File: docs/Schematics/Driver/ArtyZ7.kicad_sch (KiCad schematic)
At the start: 0 parts

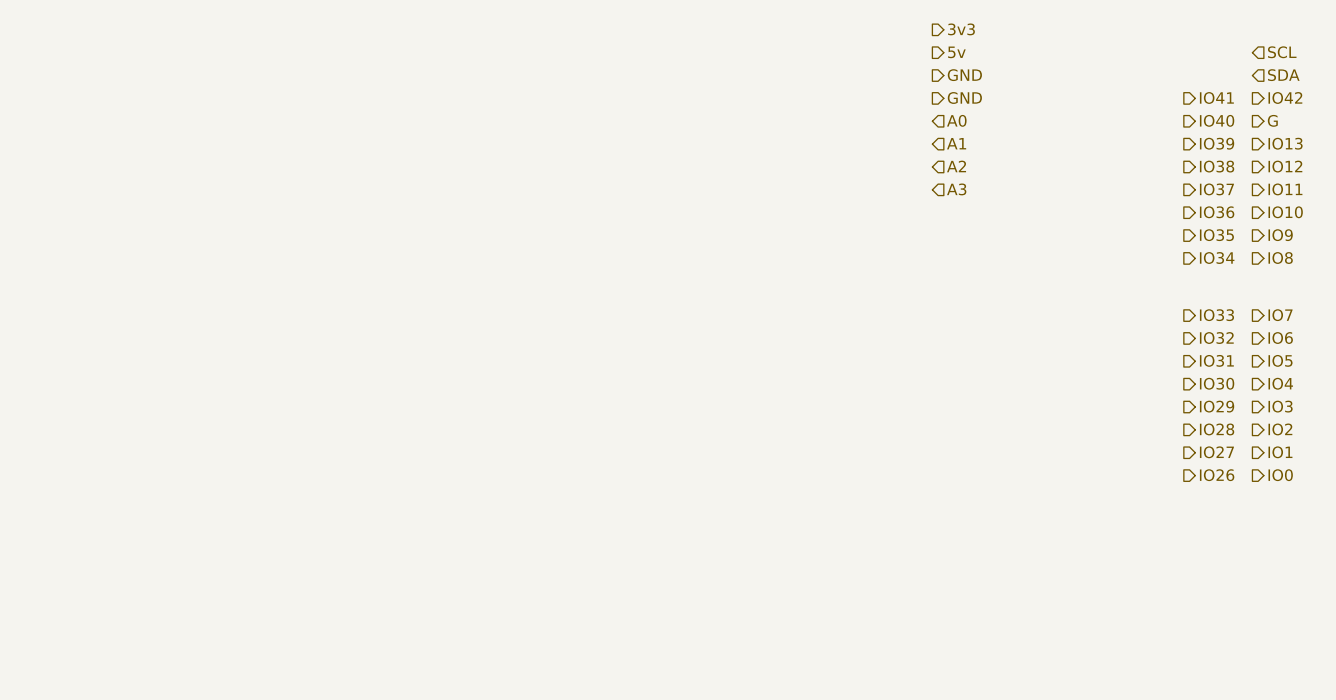
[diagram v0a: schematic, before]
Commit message: First scematic design for the card
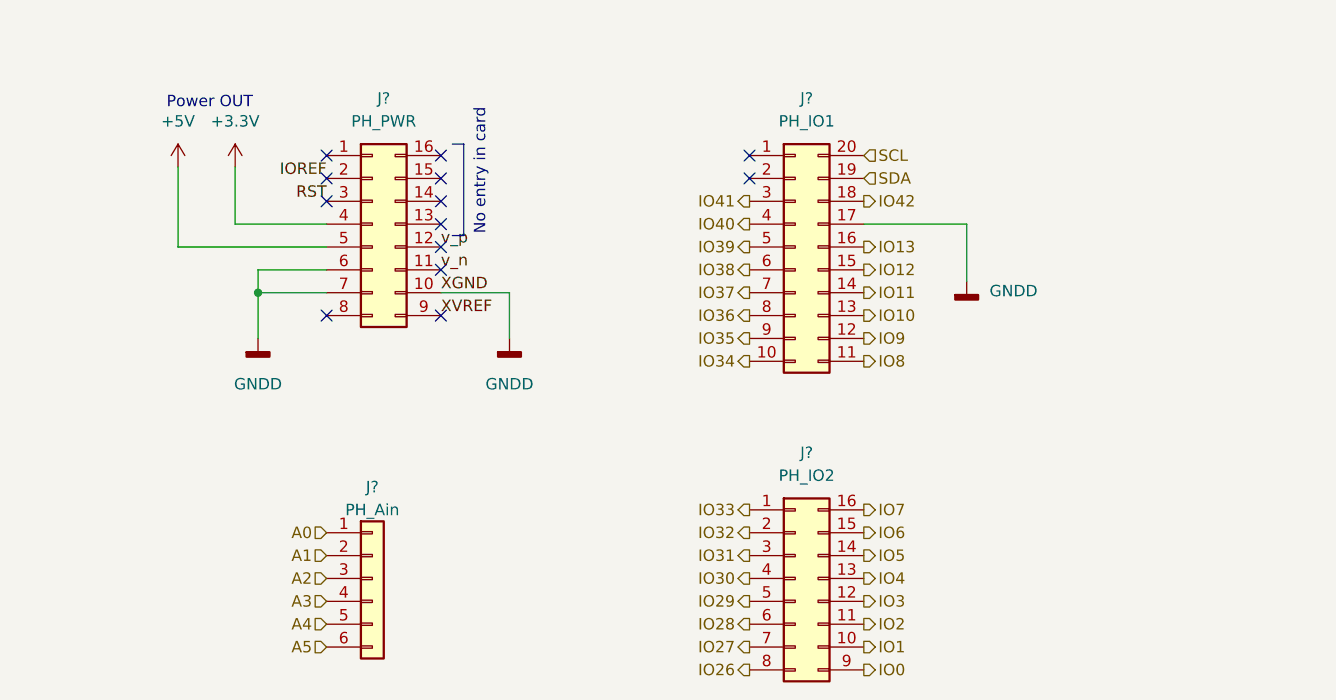
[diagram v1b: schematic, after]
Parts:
- added J?: PH_Ain, symbol Connector_Generic:Conn_01x06
- added J?: PH_IO1, symbol Connector_Generic:Conn_02x10_Counter_Clockwise
- added J?: PH_IO2, symbol Connector_Generic:Conn_02x08_Counter_Clockwise
- added J?: PH_PWR, symbol Connector_Generic:Conn_02x08_Counter_Clockwise
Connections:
- net A0: now also J?.1 (Pin_1)
- net A1: now also J?.2 (Pin_2)
- net A2: now also J?.3 (Pin_3)
- net A3: now also J?.4 (Pin_4)
- net IO0: now also J?.9 (Pin_9)
- net IO1: now also J?.10 (Pin_10)
- net IO10: now also J?.13 (Pin_13)
- net IO11: now also J?.14 (Pin_14)
- net IO12: now also J?.15 (Pin_15)
- net IO13: now also J?.16 (Pin_16)
- net IO2: now also J?.11 (Pin_11)
- net IO26: now also J?.8 (Pin_8)
- net IO27: now also J?.7 (Pin_7)
- net IO28: now also J?.6 (Pin_6)
- net IO29: now also J?.5 (Pin_5)
- net IO3: now also J?.12 (Pin_12)
- net IO30: now also J?.4 (Pin_4)
- net IO31: now also J?.3 (Pin_3)
- net IO32: now also J?.2 (Pin_2)
- net IO33: now also J?.1 (Pin_1)
- net IO34: now also J?.10 (Pin_10)
- net IO35: now also J?.9 (Pin_9)
- net IO36: now also J?.8 (Pin_8)
- net IO37: now also J?.7 (Pin_7)
- net IO38: now also J?.6 (Pin_6)
- net IO39: now also J?.5 (Pin_5)
- net IO4: now also J?.13 (Pin_13)
- net IO40: now also J?.4 (Pin_4)
- net IO41: now also J?.3 (Pin_3)
- net IO42: now also J?.18 (Pin_18)
- net IO5: now also J?.14 (Pin_14)
- net IO6: now also J?.15 (Pin_15)
- net IO7: now also J?.16 (Pin_16)
- net IO8: now also J?.11 (Pin_11)
- net IO9: now also J?.12 (Pin_12)
- net SCL: now also J?.20 (Pin_20)
- net SDA: now also J?.19 (Pin_19)
- new net +3.3V: J?.4 (Pin_4)
- new net +5V: J?.5 (Pin_5)
- new net A4: J?.5 (Pin_5)
- new net A5: J?.6 (Pin_6)
- new net GNDD: J?.10 (Pin_10), J?.17 (Pin_17), J?.6 (Pin_6), J?.7 (Pin_7)
- new net IOREF: J?.2 (Pin_2)
- new net RST: J?.3 (Pin_3)
- new net XVREF: J?.9 (Pin_9)
- new net v_n: J?.11 (Pin_11)
- new net v_p: J?.12 (Pin_12)
- no-connect marks 0 -> 13
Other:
- note added: "No entry in card"
- note added: "Power OUT"
- company: (none) -> HiQ
- title: (none) -> Arty Z7 IO expander card

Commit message: Added footprints and a symbol for the level shifters
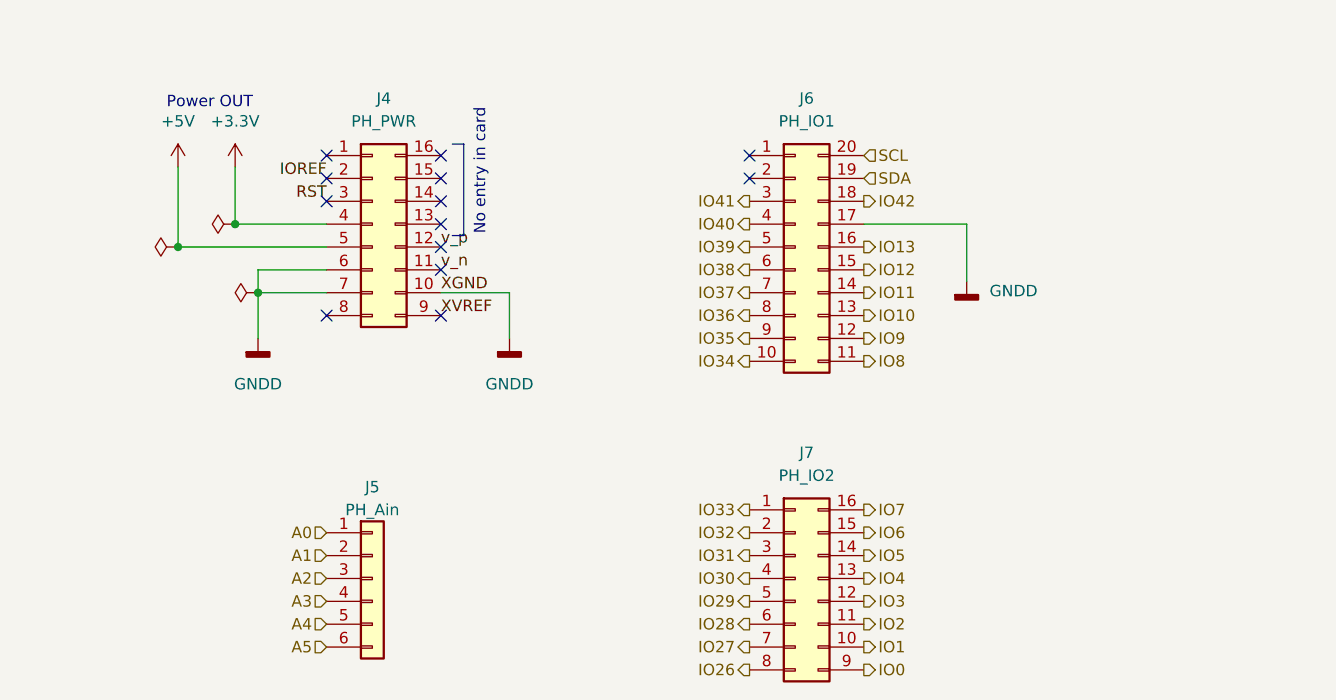
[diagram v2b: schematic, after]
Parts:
- J4, J7: renamed from J?; footprint (none) -> Connector_PinHeader_2.54mm:PinHeader_2x16_P2.54mm_Vertical
- J5: renamed from J?; footprint (none) -> Connector_PinHeader_2.54mm:PinHeader_1x06_P2.54mm_Vertical
- J6: renamed from J?; footprint (none) -> Connector_PinHeader_2.54mm:PinHeader_2x20_P2.54mm_Vertical
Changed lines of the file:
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@@
     (company "HiQ")
+  )
+  (junction (at 93.98 90.17) (diameter 0) (color 0 0 0 0)
+  )
+  (junction (at 100.33 87.63) (diameter 0) (color 0 0 0 0)
   )
   (junction (at 102.87 95.25) (diameter 0) (color 0 0 0 0)
@@
   (symbol (lib_id "power:+5V") (at 93.98 81.28 0) (unit 1)
     (in_bom yes) (on_board yes) (fields_autoplaced)
-    (property "Reference" "#PWR?" (id 0) (at 93.98 85.09 0)
+    (property "Reference" "#PWR07" (id 0) (at 93.98 85.09 0)
       (effects (font (size 1.27 1.27)) hide)
     )
@@
   (symbol (lib_id "power:+3.3V") (at 100.33 81.28 0) (unit 1)
     (in_bom yes) (on_board yes) (fields_autoplaced)
-    (property "Reference" "#PWR?" (id 0) (at 100.33 85.09 0)
+    (property "Reference" "#PWR08" (id 0) (at 100.33 85.09 0)
       (effects (font (size 1.27 1.27)) hide)
     )
@@
   (symbol (lib_id "power:GNDD") (at 181.61 93.98 0) (unit 1)
     (in_bom yes) (on_board yes) (fields_autoplaced)
-    (property "Reference" "#PWR?" (id 0) (at 181.61 100.33 0)
+    (property "Reference" "#PWR011" (id 0) (at 181.61 100.33 0)
       (effects (font (size 1.27 1.27)) hide)
     )
@@
   (symbol (lib_id "power:GNDD") (at 130.81 100.33 0) (unit 1)
     (in_bom yes) (on_board yes) (fields_autoplaced)
-    (property "Reference" "#PWR?" (id 0) (at 130.81 106.68 0)
+    (property "Reference" "#PWR010" (id 0) (at 130.81 106.68 0)
       (effects (font (size 1.27 1.27)) hide)
     )
@@
   (symbol (lib_id "Connector_Generic:Conn_01x06") (at 115.57 127 0) (unit 1)
     (in_bom yes) (on_board yes)
-    (property "Reference" "J?" (id 0) (at 115.57 116.84 0))
+    (property "Reference" "J5" (id 0) (at 115.57 116.84 0))
     (property "Value" "PH_Ain" (id 1) (at 115.57 119.38 0))
-    (property "Footprint" "" (id 2) (at 115.57 127 0)
+    (property "Footprint" "Connector_PinHeader_2.54mm:PinHeader_1x06_P2.54mm_Vertical" (id 2) (at 115.57 127 0)
       (effects (font (size 1.27 1.27)) hide)
     )
@@
     (pin "6")
   )
+  (symbol (lib_id "power:PWR_FLAG") (at 93.98 90.17 90) (unit 1)
+    (in_bom yes) (on_board yes) (fields_autoplaced)
+    (property "Reference" "#FLG0102" (id 0) (at 92.075 90.17 0)
+      (effects (font (size 1.27 1.27)) hide)
+    )
+    (property "Value" "PWR_FLAG" (id 1) (at 90.17 90.1699 90)
+      (effects (font (size 1.27 1.27)) (justify left) hide)
+    )
+    (property "Footprint" "" (id 2) (at 93.98 90.17 0)
+      (effects (font (size 1.27 1.27)) hide)
+    )
+    (property "Datasheet" "~" (id 3) (at 93.98 90.17 0)
+      (effects (font (size 1.27 1.27)) hide)
+    )
+    (pin "1")
+  )
   (symbol (lib_id "Connector_Generic:Conn_02x10_Counter_Clockwise") (at 162.56 90.17 0) (unit 1)
     (in_bom yes) (on_board yes) (fields_autoplaced)
-    (property "Reference" "J?" (id 0) (at 163.83 73.66 0))
+    (property "Reference" "J6" (id 0) (at 163.83 73.66 0))
     (property "Value" "PH_IO1" (id 1) (at 163.83 76.2 0))
-    (property "Footprint" "" (id 2) (at 162.56 90.17 0)
+    (property "Footprint" "Connector_PinHeader_2.54mm:PinHeader_2x20_P2.54mm_Vertical" (id 2) (at 162.56 90.17 0)
       (effects (font (size 1.27 1.27)) hide)
     )
@@
   (symbol (lib_id "Connector_Generic:Conn_02x08_Counter_Clockwise") (at 162.56 127 0) (unit 1)
     (in_bom yes) (on_board yes) (fields_autoplaced)
-    (property "Reference" "J?" (id 0) (at 163.83 113.03 0))
+    (property "Reference" "J7" (id 0) (at 163.83 113.03 0))
     (property "Value" "PH_IO2" (id 1) (at 163.83 115.57 0))
-    (property "Footprint" "" (id 2) (at 162.56 127 0)
+    (property "Footprint" "Connector_PinHeader_2.54mm:PinHeader_2x16_P2.54mm_Vertical" (id 2) (at 162.56 127 0)
       (effects (font (size 1.27 1.27)) hide)
     )
@@
     (pin "9")
   )
+  (symbol (lib_id "power:PWR_FLAG") (at 102.87 95.25 90) (unit 1)
+    (in_bom yes) (on_board yes) (fields_autoplaced)
+    (property "Reference" "#FLG0101" (id 0) (at 100.965 95.25 0)
+      (effects (font (size 1.27 1.27)) hide)
+    )
+    (property "Value" "PWR_FLAG" (id 1) (at 99.06 95.2499 90)
+      (effects (font (size 1.27 1.27)) (justify left) hide)
+    )
+    (property "Footprint" "" (id 2) (at 102.87 95.25 0)
+      (effects (font (size 1.27 1.27)) hide)
+    )
+    (property "Datasheet" "~" (id 3) (at 102.87 95.25 0)
+      (effects (font (size 1.27 1.27)) hide)
+    )
+    (pin "1")
+  )
+  (symbol (lib_id "power:PWR_FLAG") (at 100.33 87.63 90) (unit 1)
+    (in_bom yes) (on_board yes) (fields_autoplaced)
+    (property "Reference" "#FLG0103" (id 0) (at 98.425 87.63 0)
+      (effects (font (size 1.27 1.27)) hide)
+    )
+    (property "Value" "PWR_FLAG" (id 1) (at 96.52 87.6299 90)
+      (effects (font (size 1.27 1.27)) (justify left) hide)
+    )
+    (property "Footprint" "" (id 2) (at 100.33 87.63 0)
+      (effects (font (size 1.27 1.27)) hide)
+    )
+    (property "Datasheet" "~" (id 3) (at 100.33 87.63 0)
+      (effects (font (size 1.27 1.27)) hide)
+    )
+    (pin "1")
+  )
   (symbol (lib_id "Connector_Generic:Conn_02x08_Counter_Clockwise") (at 115.57 87.63 0) (unit 1)
     (in_bom yes) (on_board yes) (fields_autoplaced)
-    (property "Reference" "J?" (id 0) (at 116.84 73.66 0))
+    (property "Reference" "J4" (id 0) (at 116.84 73.66 0))
     (property "Value" "PH_PWR" (id 1) (at 116.84 76.2 0))
-    (property "Footprint" "" (id 2) (at 115.57 87.63 0)
+    (property "Footprint" "Connector_PinHeader_2.54mm:PinHeader_2x16_P2.54mm_Vertical" (id 2) (at 115.57 87.63 0)
       (effects (font (size 1.27 1.27)) hide)
     )
@@
   (symbol (lib_id "power:GNDD") (at 102.87 100.33 0) (unit 1)
     (in_bom yes) (on_board yes) (fields_autoplaced)
-    (property "Reference" "#PWR?" (id 0) (at 102.87 106.68 0)
-      (effects (font (size 1.27 1.27)) hide)
-    )
+    (property "Reference" "#PWR09" (id 0) (at 102.87 106.68 0)
+      (effects (font (size 1.27 1.27)) hide)
+    )

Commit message: Added caps and changed the connection from the motor sensors to plints
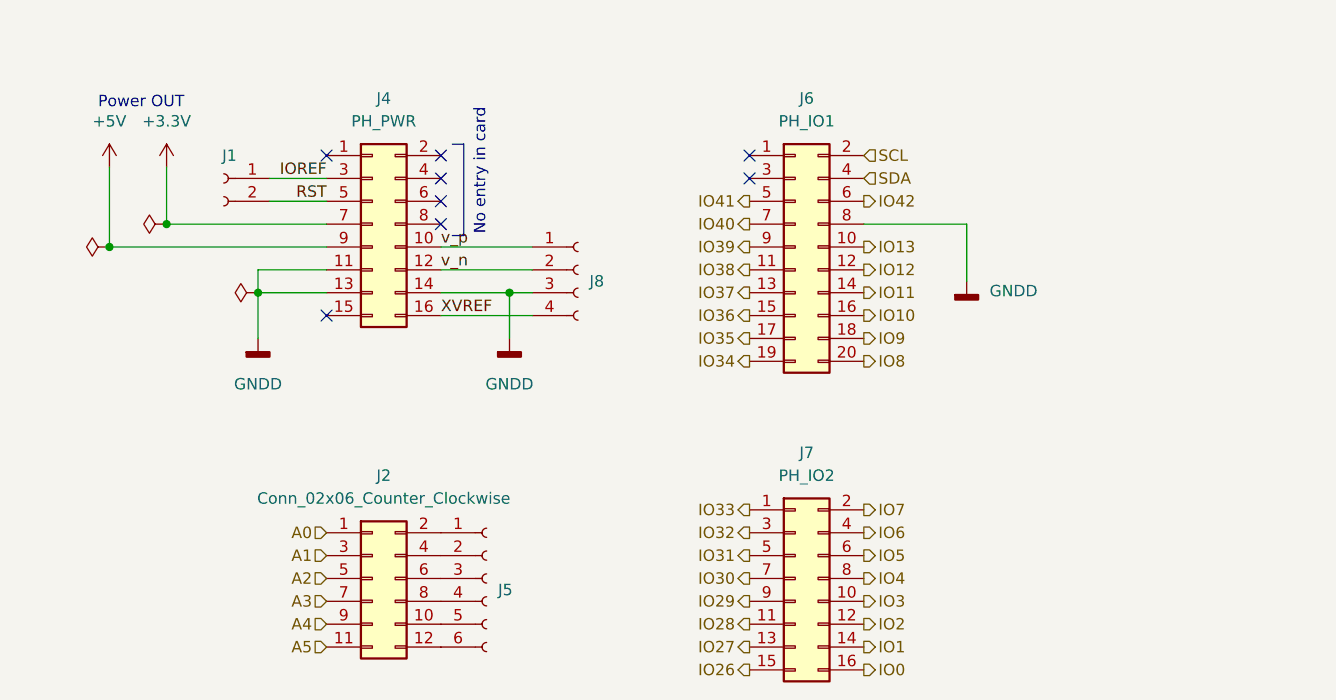
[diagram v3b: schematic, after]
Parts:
- removed J5: PH_Ain, Connector_PinHeader_2.54mm:PinHeader_1x06_P2.54mm_Vertical, symbol Connector_Generic:Conn_01x06
- added J1: Conn_01x02_Female, Connector_PinHeader_2.54mm:PinHeader_1x02_P2.54mm_Vertical, symbol Connector:Conn_01x02_Female
- added J2: Conn_02x06_Counter_Clockwise, Connector_PinHeader_2.54mm:PinHeader_2x06_P2.54mm_Vertical, symbol Connector_Generic:Conn_02x06_Odd_Even
- added J5: Conn_01x06_Female, Connector_PinSocket_2.54mm:PinSocket_1x06_P2.54mm_Vertical, symbol Connector:Conn_01x06_Female
- added J8: Conn_01x04_Female, Connector_PinSocket_2.54mm:PinSocket_1x04_P2.54mm_Vertical, symbol Connector:Conn_01x04_Female
- J4, J7: symbol Connector_Generic:Conn_02x08_Counter_Clockwise -> Connector_Generic:Conn_02x08_Odd_Even
- J6: symbol Connector_Generic:Conn_02x10_Counter_Clockwise -> Connector_Generic:Conn_02x10_Odd_Even
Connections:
- net +3.3V: now also J4.7 (Pin_7); no longer J4.4 (Pin_4)
- net +5V: now also J4.9 (Pin_9); no longer J4.5 (Pin_5)
- net A0: now also J2.1 (Pin_1)
- net A1: now also J2.3 (Pin_3)
- net A2: now also J2.5 (Pin_5)
- net A3: now also J2.7 (Pin_7)
- net A4: now also J2.9 (Pin_9)
- net A5: now also J2.11 (Pin_11)
- net GNDD: now also J4.11 (Pin_11), J4.13 (Pin_13), J4.14 (Pin_14), J6.8 (Pin_8), J8.3 (Pin_3); no longer J4.10 (Pin_10), J4.6 (Pin_6), J4.7 (Pin_7), J6.17 (Pin_17)
- net IO0: now also J7.16 (Pin_16); no longer J7.9 (Pin_9)
- net IO1: now also J7.14 (Pin_14); no longer J7.10 (Pin_10)
- net IO10: now also J6.16 (Pin_16); no longer J6.13 (Pin_13)
- net IO12: now also J6.12 (Pin_12); no longer J6.15 (Pin_15)
- net IO13: now also J6.10 (Pin_10); no longer J6.16 (Pin_16)
- net IO2: now also J7.12 (Pin_12); no longer J7.11 (Pin_11)
- net IO26: now also J7.15 (Pin_15); no longer J7.8 (Pin_8)
- net IO27: now also J7.13 (Pin_13); no longer J7.7 (Pin_7)
- net IO28: now also J7.11 (Pin_11); no longer J7.6 (Pin_6)
- net IO29: now also J7.9 (Pin_9); no longer J7.5 (Pin_5)
- net IO3: now also J7.10 (Pin_10); no longer J7.12 (Pin_12)
- net IO30: now also J7.7 (Pin_7); no longer J7.4 (Pin_4)
- net IO31: now also J7.5 (Pin_5); no longer J7.3 (Pin_3)
- net IO32: now also J7.3 (Pin_3); no longer J7.2 (Pin_2)
- net IO34: now also J6.19 (Pin_19); no longer J6.10 (Pin_10)
- net IO35: now also J6.17 (Pin_17); no longer J6.9 (Pin_9)
- net IO36: now also J6.15 (Pin_15); no longer J6.8 (Pin_8)
- net IO37: now also J6.13 (Pin_13); no longer J6.7 (Pin_7)
- net IO38: now also J6.11 (Pin_11); no longer J6.6 (Pin_6)
- net IO39: now also J6.9 (Pin_9); no longer J6.5 (Pin_5)
- net IO4: now also J7.8 (Pin_8); no longer J7.13 (Pin_13)
- net IO40: now also J6.7 (Pin_7); no longer J6.4 (Pin_4)
- net IO41: now also J6.5 (Pin_5); no longer J6.3 (Pin_3)
- net IO42: now also J6.6 (Pin_6); no longer J6.18 (Pin_18)
- net IO5: now also J7.6 (Pin_6); no longer J7.14 (Pin_14)
- net IO6: now also J7.4 (Pin_4); no longer J7.15 (Pin_15)
- net IO7: now also J7.2 (Pin_2); no longer J7.16 (Pin_16)
- net IO8: now also J6.20 (Pin_20); no longer J6.11 (Pin_11)
- net IO9: now also J6.18 (Pin_18); no longer J6.12 (Pin_12)
- net IOREF: now also J4.3 (Pin_3), J1.1 (Pin_1); no longer J4.2 (Pin_2)
- net RST: now also J4.5 (Pin_5), J1.2 (Pin_2); no longer J4.3 (Pin_3)
- net SCL: now also J6.2 (Pin_2); no longer J6.20 (Pin_20)
- net SDA: now also J6.4 (Pin_4); no longer J6.19 (Pin_19)
- net XVREF: now also J4.16 (Pin_16), J8.4 (Pin_4); no longer J4.9 (Pin_9)
- net v_n: now also J4.12 (Pin_12), J8.2 (Pin_2); no longer J4.11 (Pin_11)
- net v_p: now also J4.10 (Pin_10), J8.1 (Pin_1); no longer J4.12 (Pin_12)
- new net: J2.2 (Pin_2), J5.1 (Pin_1)
- new net: J2.4 (Pin_4), J5.2 (Pin_2)
- new net: J2.6 (Pin_6), J5.3 (Pin_3)
- new net: J2.8 (Pin_8), J5.4 (Pin_4)
- new net: J2.10 (Pin_10), J5.5 (Pin_5)
- new net: J2.12 (Pin_12), J5.6 (Pin_6)
- no-connect marks 13 -> 8
